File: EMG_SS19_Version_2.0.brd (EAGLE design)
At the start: 160 x 100 mm, 218 parts, among them T11 OPA388, T12 OPA388, T21 OPA388, T22 OPA388

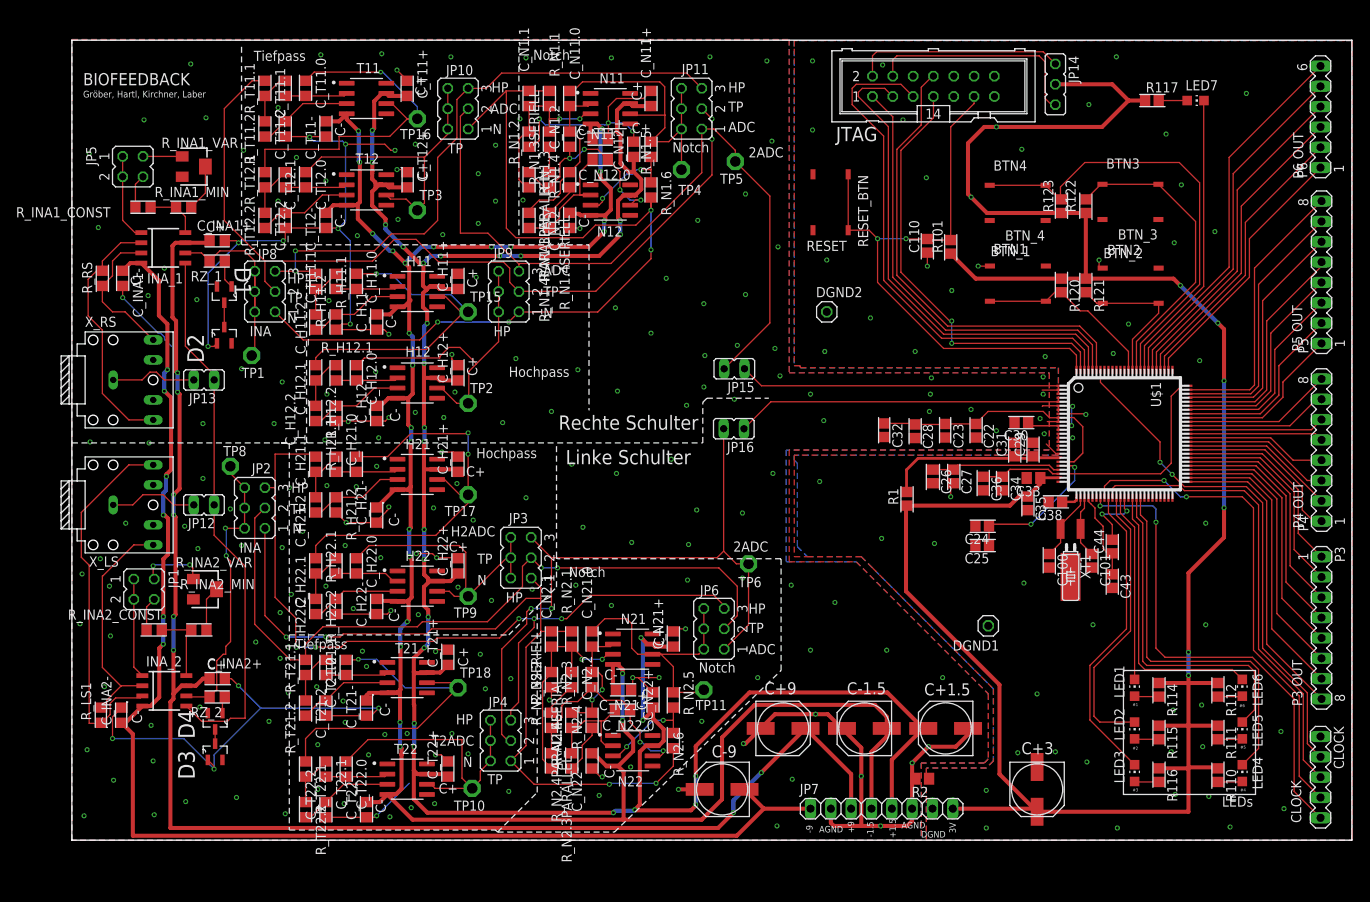
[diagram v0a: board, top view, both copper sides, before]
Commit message: rotated a pinout-connector
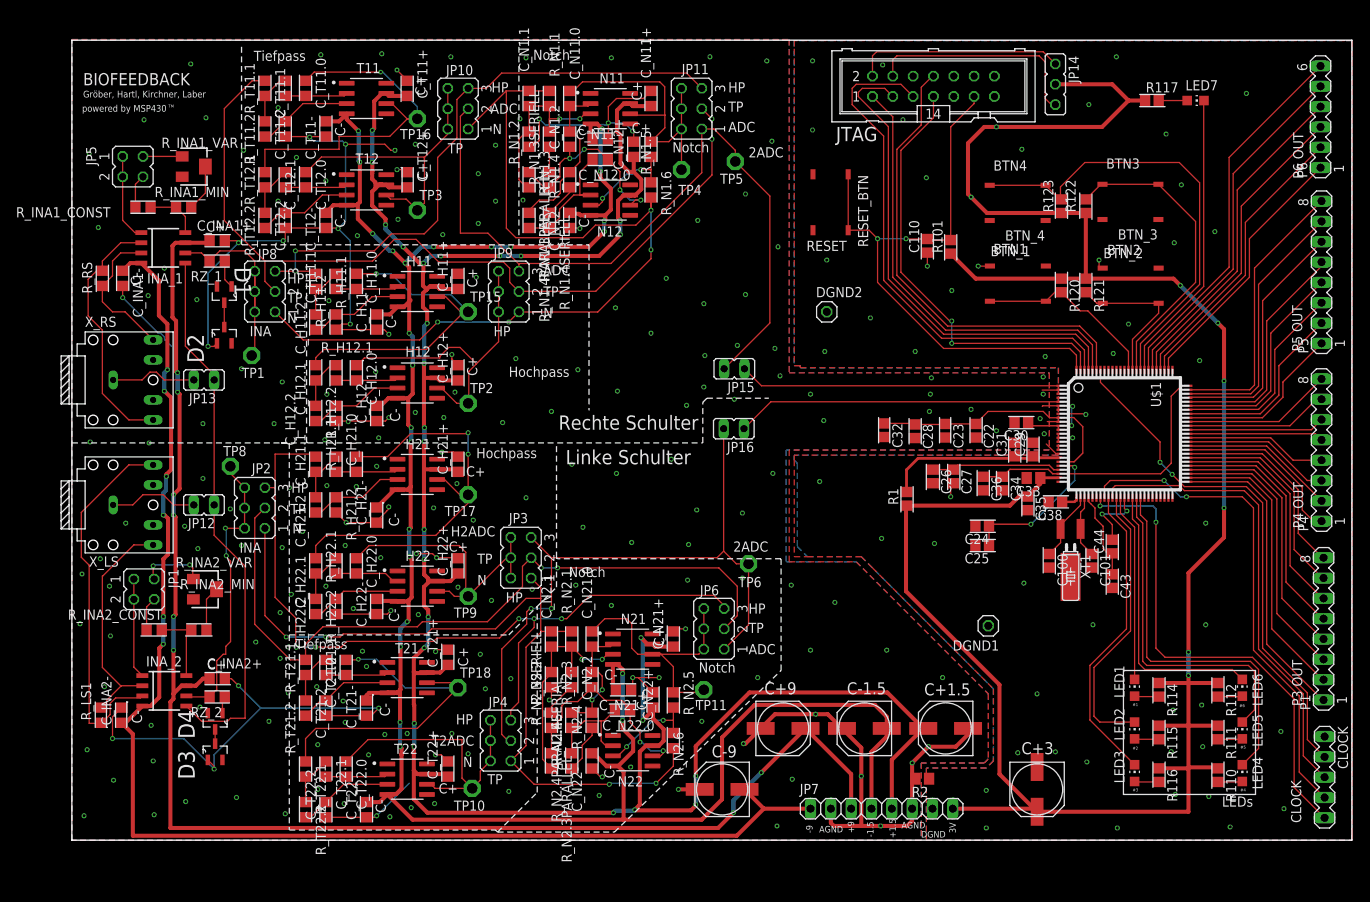
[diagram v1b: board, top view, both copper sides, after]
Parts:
- removed P3: (no value), con-lstb:MA08-1
- added P1: (no value), con-lstb:MA08-1
- moved CLOCK 0.51 mm to (156.6, 7.87)
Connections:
- removed net N$63: U$1.43
- removed net N$64: U$1.44
- removed net N$65: U$1.45
- removed net N$66: U$1.47
- removed net N$67: U$1.48
- removed net N$68: U$1.49
- removed net N$69: U$1.50
- net N$70: now also P1.1; no longer P3.8
- net N$71: now also P1.2; no longer P3.7
- net N$72: now also P1.3; no longer P3.6
- net N$73: now also P1.4; no longer P3.5
- net N$74: now also P1.5; no longer P3.4
- net N$75: now also P1.6; no longer P3.3
- net N$76: now also P1.7; no longer P3.2
- net N$77: now also P1.8; no longer P3.1
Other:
- board text added: "TM"
- board text added: "powered by MSP430"

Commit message: moved gnd and added more gnd vias
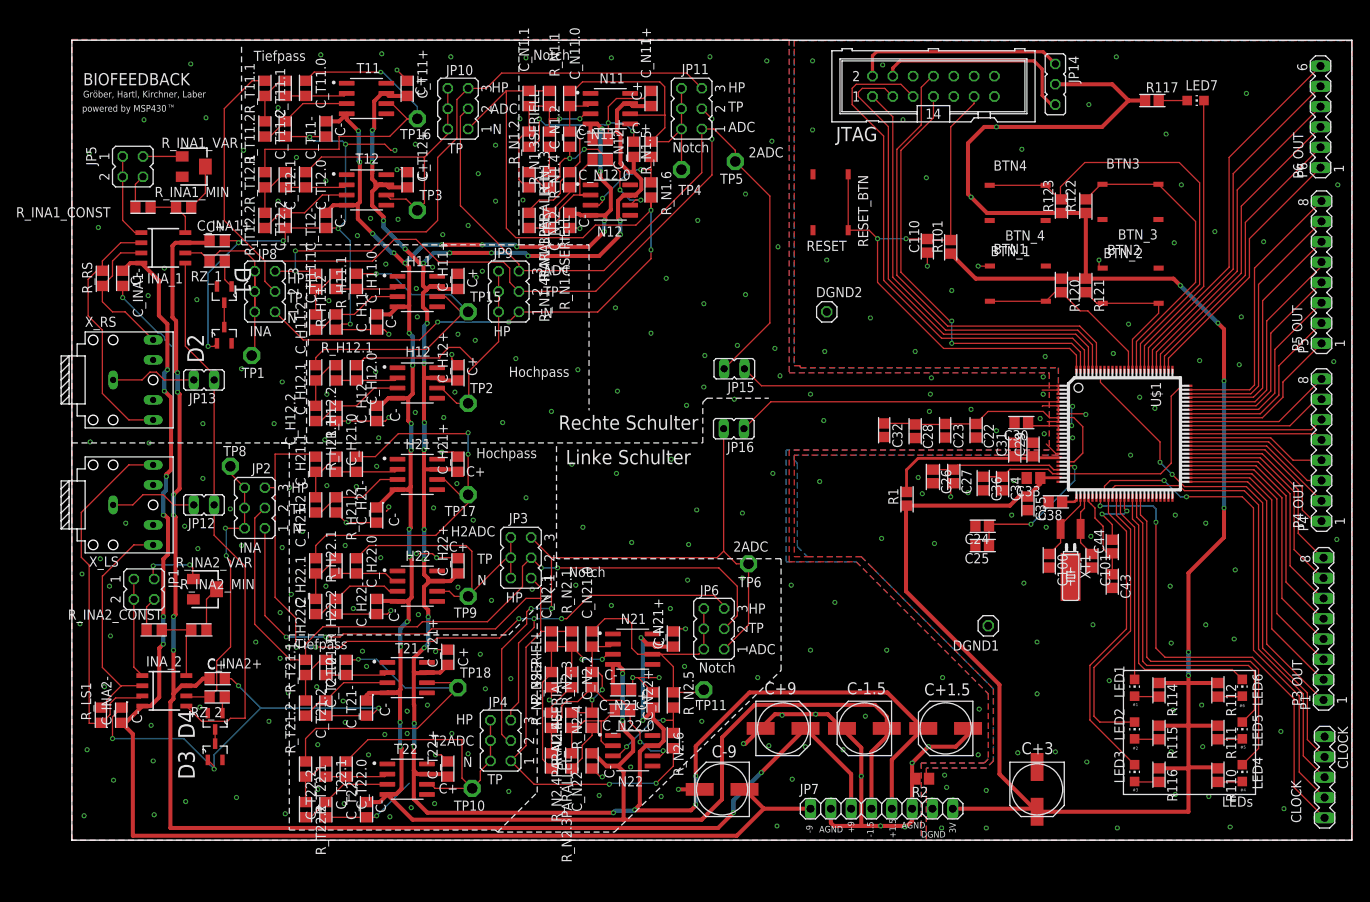
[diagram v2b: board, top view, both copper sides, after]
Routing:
- net EXT: track 27.8 -> 25.9 mm
- net AGND: track 315.4 -> 313.7 mm, vias 214 -> 235
- net RS_TO_ADC1: track 95.6 -> 94.0 mm
- net H2_OUT: track 36.9 -> 37.8 mm
- net N$27: track 11.4 -> 11.9 mm
- net DGND: vias 53 -> 79

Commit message: moved some wires for more GND-shielding, added labeling
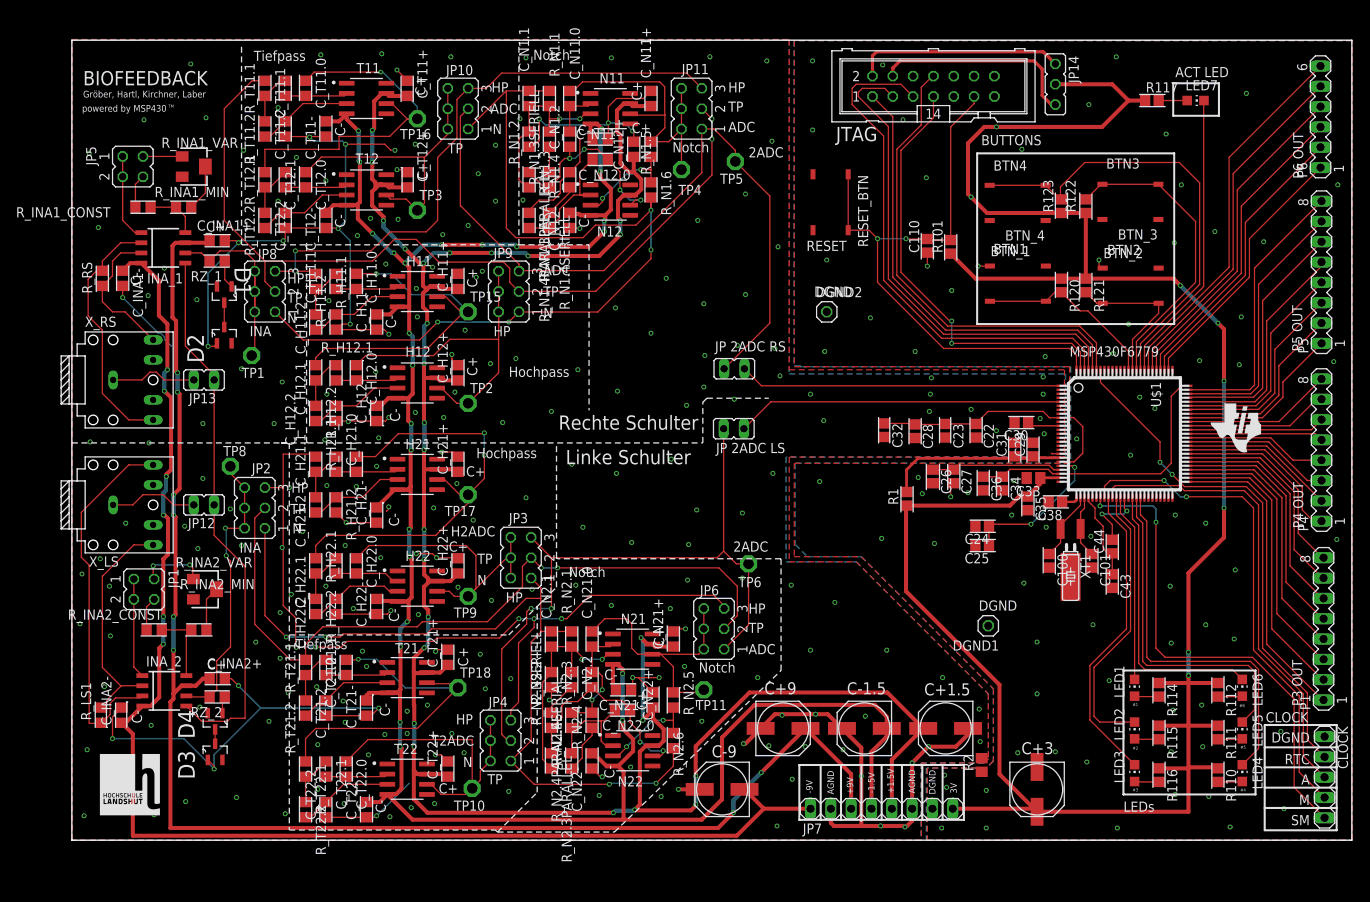
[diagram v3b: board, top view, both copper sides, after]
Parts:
- moved R2 7.62 mm to (113.7, 9.40), turned to 90 degrees
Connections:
- net AGND: now also U$1.12, U$1.13, U$1.14, U$1.15, U$1.16, U$1.17, U$1.3, U$1.4, U$1.7, U$1.8
- net DGND: no longer U$1.12, U$1.13, U$1.14, U$1.15, U$1.16, U$1.17, U$1.3, U$1.4, U$1.7, U$1.8
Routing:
- net AGND: track 313.7 -> 301.2 mm, vias 235 -> 233
- net DGND: track 20.3 -> 15.6 mm, vias 79 -> 78
- net H1_OUT: track 39.6 -> 44.0 mm
- net H21_OUT: track 51.5 -> 54.4 mm
- net T2_OUT: track 37.6 -> 38.9 mm
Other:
- board text added: "+1.5V"
- board text added: "+9V"
- board text added: "-1.5V"
- board text added: "-9V"
- board text added: "A"
- board text added: "ACT LED"
- board text added: "BUTTONS"
- board text added: "JP 2ADC LS"
- board text added: "JP 2ADC RS"
- board text added: "M"
- board text added: "MSP430F6779"
- board text added: "RTC"
- board text added: "SM"
- board text removed: "+1.5"
- board text removed: "+9"
- board text removed: "-1.5"
- board text removed: "-9"
